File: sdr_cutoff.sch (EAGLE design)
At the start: 16 parts, among them IC1 7805T, K1 HY1Z-5V

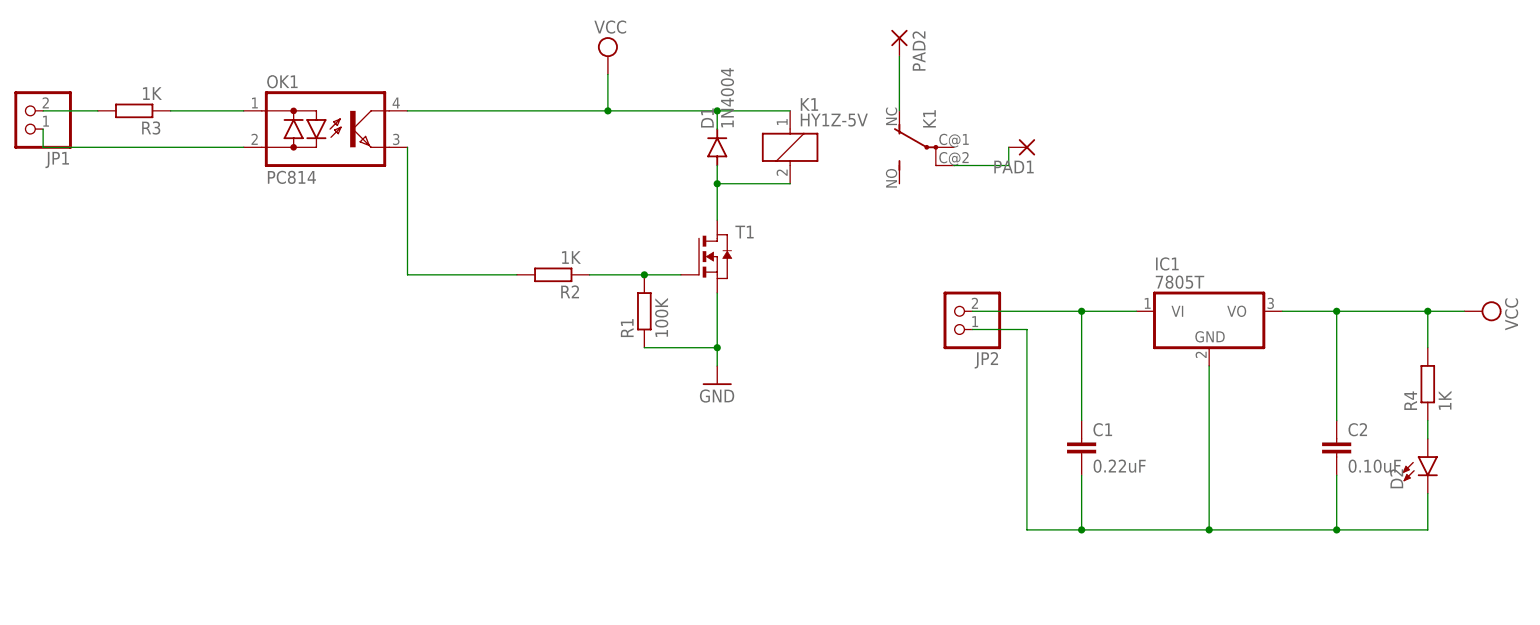
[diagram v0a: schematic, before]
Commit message: Add files via upload
Corrected missing ground on DC block
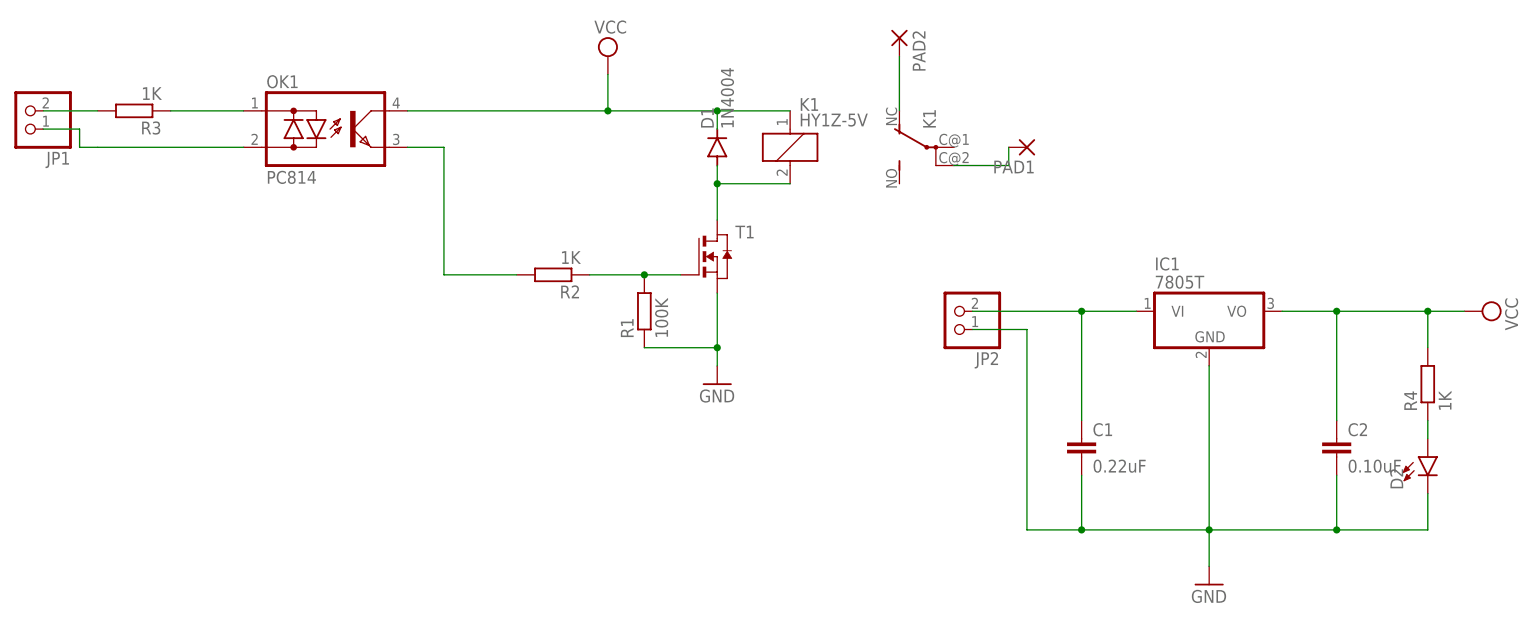
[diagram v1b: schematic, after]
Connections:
- removed net N$7: C1.2, C2.2, D2.C, IC1.GND, JP2.1
- net GND: now also C1.2, C2.2, D2.C, IC1.GND, JP2.1
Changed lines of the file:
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@@
 <part name="PAD1" library="wirepad" library_urn="urn:adsk.eagle:library:412" deviceset="2,54/0,8" device="" package3d_urn="urn:adsk.eagle:package:30838/1"/>
 <part name="PAD2" library="wirepad" library_urn="urn:adsk.eagle:library:412" deviceset="2,54/0,8" device="" package3d_urn="urn:adsk.eagle:package:30838/1"/>
+<part name="GND2" library="supply1" library_urn="urn:adsk.eagle:library:371" deviceset="GND" device=""/>
 </parts>
 <sheets>
@@
 <attribute name="VALUE" x="90.678" y="82.423" size="1.778" layer="96" rot="R270"/>
 </instance>
+<instance part="GND2" gate="1" x="137.16" y="5.08" smashed="yes">
+<attribute name="VALUE" x="134.62" y="2.54" size="1.778" layer="96"/>
+</instance>
 </instances>
 <busses>
@@
 <junction x="68.58" y="38.1"/>
 </segment>
-</net>
-<net name="VCC" class="0">
-<segment>
-<pinref part="K1" gate="1" pin="1"/>
-<wire x1="78.74" y1="71.12" x2="68.58" y2="71.12" width="0.1524" layer="91"/>
-<pinref part="D1" gate="1" pin="C"/>
-<wire x1="68.58" y1="71.12" x2="68.58" y2="68.58" width="0.1524" layer="91"/>
-<pinref part="OK1" gate="A" pin="C"/>
-<wire x1="25.4" y1="71.12" x2="53.34" y2="71.12" width="0.1524" layer="91"/>
-<junction x="68.58" y="71.12"/>
-<pinref part="SUPPLY1" gate="G$1" pin="VCC"/>
-<wire x1="53.34" y1="71.12" x2="68.58" y2="71.12" width="0.1524" layer="91"/>
-<wire x1="53.34" y1="76.2" x2="53.34" y2="71.12" width="0.1524" layer="91"/>
-<junction x="53.34" y="71.12"/>
-</segment>
-<segment>
-<pinref part="IC1" gate="A1" pin="VO"/>
-<wire x1="147.32" y1="43.18" x2="154.94" y2="43.18" width="0.1524" layer="91"/>
-<pinref part="C2" gate="G$1" pin="1"/>
-<wire x1="154.94" y1="43.18" x2="167.64" y2="43.18" width="0.1524" layer="91"/>
-<wire x1="167.64" y1="43.18" x2="172.72" y2="43.18" width="0.1524" layer="91"/>
-<wire x1="154.94" y1="27.94" x2="154.94" y2="43.18" width="0.1524" layer="91"/>
-<junction x="154.94" y="43.18"/>
-<pinref part="SUPPLY3" gate="G$1" pin="VCC"/>
-<pinref part="R4" gate="G$1" pin="2"/>
-<wire x1="167.64" y1="38.1" x2="167.64" y2="43.18" width="0.1524" layer="91"/>
-<junction x="167.64" y="43.18"/>
-</segment>
-</net>
-<net name="N$2" class="0">
-<segment>
-<pinref part="OK1" gate="A" pin="E"/>
-<wire x1="25.4" y1="66.04" x2="25.4" y2="48.26" width="0.1524" layer="91"/>
-<pinref part="R2" gate="G$1" pin="2"/>
-<wire x1="25.4" y1="48.26" x2="40.64" y2="48.26" width="0.1524" layer="91"/>
-</segment>
-</net>
-<net name="N$4" class="0">
-<segment>
-<pinref part="R3" gate="G$1" pin="1"/>
-<pinref part="OK1" gate="A" pin="AC1"/>
-<wire x1="-7.62" y1="71.12" x2="2.54" y2="71.12" width="0.1524" layer="91"/>
-</segment>
-</net>
-<net name="N$5" class="0">
-<segment>
-<pinref part="OK1" gate="A" pin="AC2"/>
-<wire x1="2.54" y1="66.04" x2="-25.4" y2="66.04" width="0.1524" layer="91"/>
-<pinref part="JP1" gate="G$1" pin="1"/>
-<wire x1="-25.4" y1="66.04" x2="-25.4" y2="68.58" width="0.1524" layer="91"/>
-</segment>
-</net>
-<net name="N$6" class="0">
-<segment>
-<pinref part="R3" gate="G$1" pin="2"/>
-<pinref part="JP1" gate="G$1" pin="2"/>
-<wire x1="-17.78" y1="71.12" x2="-25.4" y2="71.12" width="0.1524" layer="91"/>
-</segment>
-</net>
-<net name="N$7" class="0">
 <segment>
 <pinref part="IC1" gate="A1" pin="GND"/>
@@
 <junction x="119.38" y="12.7"/>
 <junction x="137.16" y="12.7"/>
-</segment>
-</net>
+<pinref part="GND2" gate="1" pin="GND"/>
+<wire x1="137.16" y1="12.7" x2="137.16" y2="7.62" width="0.1524" layer="91"/>
+</segment>
+</net>
+<net name="VCC" class="0">
+<segment>
+<pinref part="K1" gate="1" pin="1"/>
+<wire x1="78.74" y1="71.12" x2="68.58" y2="71.12" width="0.1524" layer="91"/>
+<pinref part="D1" gate="1" pin="C"/>
+<wire x1="68.58" y1="71.12" x2="68.58" y2="68.58" width="0.1524" layer="91"/>
+<pinref part="OK1" gate="A" pin="C"/>
+<wire x1="25.4" y1="71.12" x2="53.34" y2="71.12" width="0.1524" layer="91"/>
+<junction x="68.58" y="71.12"/>
+<pinref part="SUPPLY1" gate="G$1" pin="VCC"/>
+<wire x1="53.34" y1="71.12" x2="68.58" y2="71.12" width="0.1524" layer="91"/>
+<wire x1="53.34" y1="76.2" x2="53.34" y2="71.12" width="0.1524" layer="91"/>
+<junction x="53.34" y="71.12"/>
+</segment>
+<segment>
+<pinref part="IC1" gate="A1" pin="VO"/>
+<wire x1="147.32" y1="43.18" x2="154.94" y2="43.18" width="0.1524" layer="91"/>
+<pinref part="C2" gate="G$1" pin="1"/>
+<wire x1="154.94" y1="43.18" x2="167.64" y2="43.18" width="0.1524" layer="91"/>
+<wire x1="167.64" y1="43.18" x2="172.72" y2="43.18" width="0.1524" layer="91"/>
+<wire x1="154.94" y1="27.94" x2="154.94" y2="43.18" width="0.1524" layer="91"/>
+<junction x="154.94" y="43.18"/>
+<pinref part="SUPPLY3" gate="G$1" pin="VCC"/>
+<pinref part="R4" gate="G$1" pin="2"/>
+<wire x1="167.64" y1="38.1" x2="167.64" y2="43.18" width="0.1524" layer="91"/>
+<junction x="167.64" y="43.18"/>
+</segment>
+</net>
+<net name="N$2" class="0">
+<segment>
+<pinref part="OK1" gate="A" pin="E"/>
+<wire x1="25.4" y1="66.04" x2="30.48" y2="66.04" width="0.1524" layer="91"/>
+<wire x1="30.48" y1="66.04" x2="30.48" y2="48.26" width="0.1524" layer="91"/>
+<pinref part="R2" gate="G$1" pin="2"/>
+<wire x1="30.48" y1="48.26" x2="40.64" y2="48.26" width="0.1524" layer="91"/>
+</segment>
+</net>
+<net name="N$4" class="0">
+<segment>
+<pinref part="R3" gate="G$1" pin="1"/>
+<pinref part="OK1" gate="A" pin="AC1"/>
+<wire x1="-7.62" y1="71.12" x2="2.54" y2="71.12" width="0.1524" layer="91"/>
+</segment>
+</net>
+<net name="N$5" class="0">
+<segment>
+<pinref part="OK1" gate="A" pin="AC2"/>
+<wire x1="2.54" y1="66.04" x2="-17.78" y2="66.04" width="0.1524" layer="91"/>
+<pinref part="JP1" gate="G$1" pin="1"/>
+<wire x1="-17.78" y1="66.04" x2="-20.32" y2="66.04" width="0.1524" layer="91"/>
+<wire x1="-20.32" y1="66.04" x2="-20.32" y2="68.58" width="0.1524" layer="91"/>
+<wire x1="-20.32" y1="68.58" x2="-25.4" y2="68.58" width="0.1524" layer="91"/>
+</segment>
+</net>
+<net name="N$6" class="0">
+<segment>
+<pinref part="R3" gate="G$1" pin="2"/>
+<pinref part="JP1" gate="G$1" pin="2"/>
+<wire x1="-17.78" y1="71.12" x2="-25.4" y2="71.12" width="0.1524" layer="91"/>
+</segment>
+</net>
